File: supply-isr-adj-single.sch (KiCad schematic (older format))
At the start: 26 parts, among them P1 CONN_02X02, P2 CONN_01X03, P3 CONN_02X04, P4 CONN_02X08, U1 TPS54232

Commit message: Clean up
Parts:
- gave numbers to parts that had none: 2
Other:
- moved on the sheet: C1, C2, C3, C4, C5, C6, D1, L1, P1, P2, P3, P4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

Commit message: Finalize schematic
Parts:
- C1, C6: footprint (none) -> Capacitors_SMD:C_1206
- C2: footprint (none) -> Capacitors_SMD:C_0603
- C3, C4: footprint (none) -> Capacitors_SMD:C_0402
- C5: footprint (none) -> Capacitors_SMD:C_0805
- D1: footprint (none) -> Diodes_SMD:SOD-123
- L1: footprint (none) -> custom:SRP1038A
- P1: footprint (none) -> Pin_Headers:Pin_Header_Straight_2x02
- P2: footprint (none) -> Pin_Headers:Pin_Header_Straight_1x03
- P3: footprint (none) -> Pin_Headers:Pin_Header_Straight_2x04
- P4: footprint (none) -> Pin_Headers:Pin_Header_Straight_2x08
- P5, P6: footprint (none) -> Connect:1pin
- R1: renamed from R4; footprint (none) -> Resistors_SMD:R_0402
- R10: renamed from R3; value RC0603FR-074R02L -> RC0603FR-074K02L; footprint (none) -> Resistors_SMD:R_0603
- R11: renamed from R1; footprint (none) -> Resistors_SMD:R_0402
- R2: renamed from R5; footprint (none) -> Resistors_SMD:R_0402
- R3: renamed from R6; value RC0805FR-078R06L -> RC0805FR-078K06L; footprint (none) -> Resistors_SMD:R_0805
- R4: renamed from R7; value RC0603FR-074R02L -> RC0603FR-074K02L; footprint (none) -> Resistors_SMD:R_0603
- R5: renamed from R8; footprint (none) -> Resistors_SMD:R_0805
- R6: renamed from R9; footprint (none) -> Resistors_SMD:R_0402
- R7: renamed from R10; footprint (none) -> Resistors_SMD:R_0402
- R8: renamed from R11; footprint (none) -> Resistors_SMD:R_0402
- R9: renamed from R2; value RC0402FR-0717R4L -> RC0402FR-0717K4L; footprint (none) -> Resistors_SMD:R_0402
- U1: value TPS54232 -> TPS54232DR; footprint (none) -> SMD_Packages:SOIC-8-N
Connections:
- net GND: now also P4.1 (P1), P4.11 (P11), P4.13 (P13), P4.15 (P15), P4.3 (P3), P4.5 (P5), P4.7 (P7), P4.9 (P9); no longer R1.1, R2.1, R3.1, R4.1, R5.1, R6.1, R7.1, R8.1
- net at R5.2: now also R1.2, R10.2, R2.2, R3.2, R4.2, R6.2, R7.2, R8.2, U1.5 (VSENSE); no longer P4.10 (P10)
- net at P4.12 (P12): now also R3.1; no longer R6.2
- net at P4.14 (P14): now also R2.1; no longer R7.2
- net at P4.16 (P16): now also R1.1; no longer R8.2
- net at P4.2 (P2): now also R8.1; no longer R1.2
- net at P4.4 (P4): now also R7.1; no longer R2.2
- net at P4.6 (P6): now also R6.1; no longer R3.2
- net at P4.8 (P8): now also R5.1; no longer R4.2
- new net: P4.10 (P10), R4.1
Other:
- moved on the sheet: P4, R1, R2, R3, R4, R5, R6, R7, R8

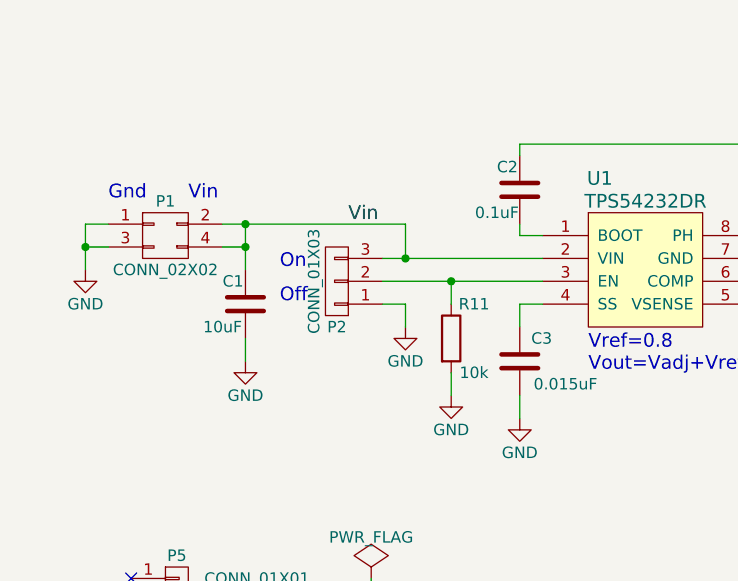
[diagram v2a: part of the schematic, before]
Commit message: Limit EN pin voltage Add LED port
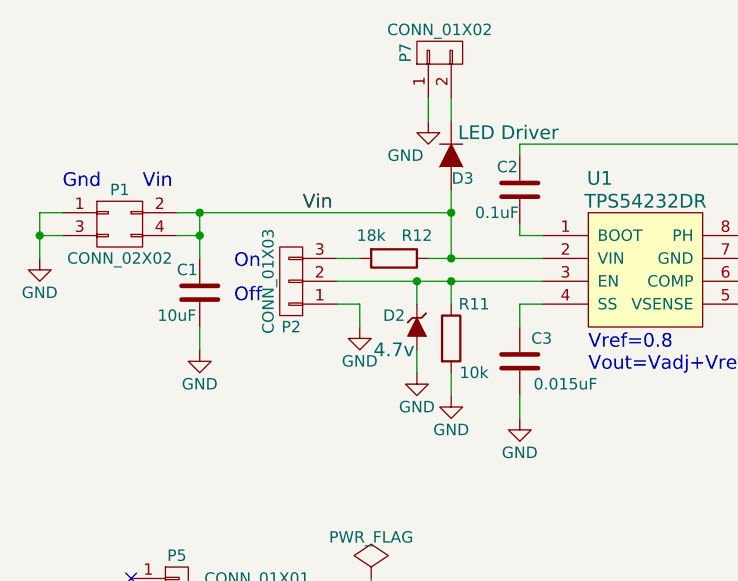
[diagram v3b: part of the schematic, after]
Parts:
- added D2: DZ2J047M0L, Diodes_SMD:SOD-323, symbol ZENERsmall
- added D3: NSI45015WT1G, Diodes_SMD:SOD-123, symbol D
- added P7: CONN_01X02, Pin_Headers:Pin_Header_Straight_1x02, symbol CONN_01X02
- added R12: RC0603FR-0717K8L, Resistors_SMD:R_0603, symbol R
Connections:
- net GND: now also D2.2 (A), P7.1 (P1)
- net Vin: now also D3.2 (A), R12.1; no longer P2.3 (P3)
- net at P2.2 (P2), R11.1, U1.3 (EN): now also D2.1 (K)
- new net: P2.3 (P3), R12.2
- new net: D3.1 (K), P7.2 (P2)
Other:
- moved on the sheet: C1, P1, P2
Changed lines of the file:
@@
 L CONN_01X03 P2
 U 1 1 57672F6C
-P 2250 1800
-F 0 "P2" H 2250 2000 50  0000 C CNN
-F 1 "CONN_01X03" V 2350 1800 50  0000 C CNN
-F 2 "Pin_Headers:Pin_Header_Straight_1x03" H 2250 1800 50  0001 C CNN
-F 3 "" H 2250 1800 50  0000 C CNN
-	1    2250 1800
+P 2050 1800
+F 0 "P2" H 2050 2000 50  0000 C CNN
+F 1 "CONN_01X03" V 2150 1800 50  0000 C CNN
+F 2 "Pin_Headers:Pin_Header_Straight_1x03" H 2050 1800 50  0001 C CNN
+F 3 "" H 2050 1800 50  0000 C CNN
+	1    2050 1800
 	-1   0    0    1
 $EndComp
@@
 L GND #PWR06
 U 1 1 57672FD7
-P 2550 2000
-F 0 "#PWR06" H 2550 1750 50  0001 C CNN
-F 1 "GND" H 2550 1850 50  0000 C CNN
-F 2 "" H 2550 2000 50  0000 C CNN
-F 3 "" H 2550 2000 50  0000 C CNN
-	1    2550 2000
+P 2350 2000
+F 0 "#PWR06" H 2350 1750 50  0001 C CNN
+F 1 "GND" H 2350 1850 50  0000 C CNN
+F 2 "" H 2350 2000 50  0000 C CNN
+F 3 "" H 2350 2000 50  0000 C CNN
+	1    2350 2000
 	1    0    0    -1
 $EndComp
@@
 L C C1
 U 1 1 576735E0
-P 1850 1900
-F 0 "C1" H 1750 2000 50  0000 L CNN
-F 1 "GRM319R6YA106KA12D" H 1875 1800 50  0001 L CNN
-F 2 "Capacitors_SMD:C_1206" H 1888 1750 50  0001 C CNN
-F 3 "" H 1850 1900 50  0000 C CNN
-F 4 "10uF" H 1750 1800 50  0000 C CNN "C"
-	1    1850 1900
+P 1650 1850
+F 0 "C1" H 1550 1950 50  0000 L CNN
+F 1 "GRM319R6YA106KA12D" H 1675 1750 50  0001 L CNN
+F 2 "Capacitors_SMD:C_1206" H 1688 1700 50  0001 C CNN
+F 3 "" H 1650 1850 50  0000 C CNN
+F 4 "10uF" H 1550 1750 50  0000 C CNN "C"
+	1    1650 1850
 	1    0    0    -1
 $EndComp
@@
 L CONN_02X02 P1
 U 1 1 5767375D
-P 1500 1600
-F 0 "P1" H 1500 1750 50  0000 C CNN
-F 1 "CONN_02X02" H 1500 1450 50  0000 C CNN
-F 2 "Pin_Headers:Pin_Header_Straight_2x02" H 1500 400 50  0001 C CNN
-F 3 "" H 1500 400 50  0000 C CNN
-	1    1500 1600
+P 1300 1550
+F 0 "P1" H 1300 1700 50  0000 C CNN
+F 1 "CONN_02X02" H 1300 1400 50  0000 C CNN
+F 2 "Pin_Headers:Pin_Header_Straight_2x02" H 1300 350 50  0001 C CNN
+F 3 "" H 1300 350 50  0000 C CNN
+	1    1300 1550
 	1    0    0    -1
 $EndComp
@@
 L GND #PWR07
 U 1 1 576739D7
-P 1150 1750
-F 0 "#PWR07" H 1150 1500 50  0001 C CNN
-F 1 "GND" H 1150 1600 50  0000 C CNN
-F 2 "" H 1150 1750 50  0000 C CNN
-F 3 "" H 1150 1750 50  0000 C CNN
-	1    1150 1750
+P 950 1700
+F 0 "#PWR07" H 950 1450 50  0001 C CNN
+F 1 "GND" H 950 1550 50  0000 C CNN
+F 2 "" H 950 1700 50  0000 C CNN
+F 3 "" H 950 1700 50  0000 C CNN
+	1    950  1700
 	1    0    0    -1
 $EndComp
@@
 L GND #PWR08
 U 1 1 57673B99
-P 1850 2150
-F 0 "#PWR08" H 1850 1900 50  0001 C CNN
-F 1 "GND" H 1850 2000 50  0000 C CNN
-F 2 "" H 1850 2150 50  0000 C CNN
-F 3 "" H 1850 2150 50  0000 C CNN
-	1    1850 2150
+P 1650 2100
+F 0 "#PWR08" H 1650 1850 50  0001 C CNN
+F 1 "GND" H 1650 1950 50  0000 C CNN
+F 2 "" H 1650 2100 50  0000 C CNN
+F 3 "" H 1650 2100 50  0000 C CNN
+	1    1650 2100
 	1    0    0    -1
 $EndComp
@@
 	1    0    0    -1
 $EndComp
-Text Label 2300 1550 0    60   ~ 0
+Text Label 2100 1500 0    60   ~ 0
 Vin
-Text Notes 1600 1450 0    60   ~ 0
+Text Notes 1400 1400 0    60   ~ 0
 Vin
-Text Notes 1250 1450 0    60   ~ 0
+Text Notes 1050 1400 0    60   ~ 0
 Gnd
-Text Notes 2000 1750 0    60   ~ 0
+Text Notes 1800 1750 0    60   ~ 0
 On
-Text Notes 2000 1900 0    60   ~ 0
+Text Notes 1800 1900 0    60   ~ 0
 Off
 Text Label 5100 1200 0    60   ~ 0
@@
 	3050 2400 3050 2300
 Wire Wire Line
-	2450 1900 2550 1900
-Wire Wire Line
-	2550 1900 2550 2000
-Wire Wire Line
-	2550 1550 2550 1700
-Connection ~ 2550 1700
-Wire Wire Line
-	1750 1650 1850 1650
-Wire Wire Line
-	1850 1550 1850 1750
-Connection ~ 1850 1550
-Wire Wire Line
-	1150 1550 1150 1750
-Wire Wire Line
-	1150 1550 1250 1550
-Wire Wire Line
-	1250 1650 1150 1650
-Connection ~ 1150 1650
-Wire Wire Line
-	1850 2150 1850 2050
-Connection ~ 1850 1650
-Wire Wire Line
-	2450 1700 3150 1700
-Wire Wire Line
-	2450 1800 3150 1800
+	2250 1900 2350 1900
+Wire Wire Line
+	2350 1900 2350 2000
+Wire Wire Line
+	1550 1600 1650 1600
+Wire Wire Line
+	1650 1500 1650 1700
+Connection ~ 1650 1500
+Wire Wire Line
+	950  1500 950  1700
+Wire Wire Line
+	950  1500 1050 1500
+Wire Wire Line
+	1050 1600 950  1600
+Connection ~ 950  1600
+Wire Wire Line
+	1650 2100 1650 2000
+Connection ~ 1650 1600
+Wire Wire Line
+	2250 1800 3150 1800
 Wire Wire Line
 	5350 1900 5350 2700
@@
 	3050 1200 4400 1200
 Wire Wire Line
-	1750 1550 2550 1550
-Wire Wire Line
 	2750 2200 2750 2300
 Wire Wire Line
@@
 Wire Wire Line
 	6400 2700 6500 2700
+Wire Wire Line
+	2650 1700 3150 1700
+Wire Wire Line
+	2600 1900 2600 1800
+Connection ~ 2600 1800
+$Comp
+L ZENERsmall D2
+U 1 1 579A55E3
+P 2600 2000
+F 0 "D2" V 2550 1900 50  0000 C CNN
+F 1 "DZ2J047M0L" H 2600 1900 50  0001 C CNN
+F 2 "Diodes_SMD:SOD-323" H 2600 2000 50  0001 C CNN
+F 3 "" H 2600 2000 50  0000 C CNN
+F 4 "4.7v" V 2700 1900 60  0000 C CNN "D"
+	1    2600 2000
+	0    1    1    0
+$EndComp
+$Comp
+L GND #PWR012
+U 1 1 579A5B1C
+P 2600 2200
+F 0 "#PWR012" H 2600 1950 50  0001 C CNN
+F 1 "GND" H 2600 2050 50  0000 C CNN
+F 2 "" H 2600 2200 50  0000 C CNN
+F 3 "" H 2600 2200 50  0000 C CNN
+	1    2600 2200
+	1    0    0    -1
+$EndComp
+Wire Wire Line
+	2600 2200 2600 2100
+$Comp
+L R R12
+U 1 1 579A5D25
+P 2500 1700
+F 0 "R12" V 2400 1800 50  0000 C CNN
+F 1 "RC0603FR-0717K8L" V 2500 1700 50  0001 C CNN
+F 2 "Resistors_SMD:R_0603" V 2430 1700 50  0001 C CNN
+F 3 "" H 2500 1700 50  0000 C CNN
+F 4 "18k" V 2400 1600 50  0000 C CNN "R"
+	1    2500 1700
+	0    1    1    0
+$EndComp
+Wire Wire Line
+	1550 1500 2750 1500
+Connection ~ 2750 1700
+Wire Wire Line
+	2350 1700 2250 1700
+Wire Wire Line
+	2750 1400 2750 1700
+$Comp
+L D D3
+U 1 1 579B72D2
+P 2750 1250
+F 0 "D3" V 2850 1300 50  0000 C CNN
+F 1 "NSI45015WT1G" H 2750 1150 50  0001 C CNN
+F 2 "Diodes_SMD:SOD-123" H 2750 1250 50  0001 C CNN
+F 3 "" H 2750 1250 50  0000 C CNN
+F 4 "LED Driver" V 2650 1500 60  0000 C CNN "D"
+	1    2750 1250
+	0    1    1    0
+$EndComp
+Connection ~ 2750 1500
+$Comp
+L CONN_01X02 P7
+U 1 1 579B73FB
+P 2700 800
+F 0 "P7" H 2700 950 50  0000 C CNN
+F 1 "CONN_01X02" V 2800 800 50  0000 C CNN
+F 2 "Pin_Headers:Pin_Header_Straight_1x02" H 2700 800 50  0001 C CNN
+F 3 "" H 2700 800 50  0000 C CNN
+	1    2700 800
+	0    -1   -1   0
+$EndComp
+Wire Wire Line
+	2750 1100 2750 1000
+$Comp
+L GND #PWR013
+U 1 1 579B77AC
+P 2650 1100
+F 0 "#PWR013" H 2650 850 50  0001 C CNN
+F 1 "GND" H 2550 950 50  0000 C CNN
+F 2 "" H 2650 1100 50  0000 C CNN
+F 3 "" H 2650 1100 50  0000 C CNN
+	1    2650 1100
+	1    0    0    -1
+$EndComp
+Wire Wire Line
+	2650 1000 2650 1100
 $EndSCHEMATC
